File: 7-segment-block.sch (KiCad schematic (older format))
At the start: 5 parts, among them J1 DATA_OUT, J2 DATA_IN, U1 TPIC6C596PWR

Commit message: Add mounting holes, dropper resistors and a buffer
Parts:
- added MK1, MK2, MK3, MK4: Mounting_Hole, Mounting_Holes:MountingHole_3.2mm_M3, symbol Mechanical:Mounting_Hole
- added R1, R2, R3, R4, R5, R6, R7, R8: 100, Resistors_SMD:R_0805_HandSoldering, symbol device:R_Small
- added U?: 74LS125, Housings_SOIC:SOIC-14_3.9x8.7mm_Pitch1.27mm, symbol Logic_74xx:74LS125
- added U? (x3): 74LS125, symbol Logic_74xx:74LS125
- C1: footprint (none) -> Capacitors_SMD:C_0805_HandSoldering; Distributor (none) -> ?; Manufacturer (none) -> ?; PartNo (none) -> ?
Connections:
- net GND: now also J1.7 (Pin_7), J2.7 (Pin_7), U?.1, U?.10, U?.13, U?.4; no longer J1.8 (Pin_8), J2.8 (Pin_8)
- net RCK: now also U?.5; no longer J1.4 (Pin_4)
- net SRCK: now also U?.9; no longer J1.6 (Pin_6)
- net VCC: now also AFF1.1 (C.A.), AFF1.8 (C.A.)
- net ~G: now also J2.8 (Pin_8), U?.12; no longer J1.7 (Pin_7), J2.7 (Pin_7)
- net at AFF1.10 (g): now also R5.1; no longer U1.11 (DRAIN4)
- net at AFF1.2 (e): now also R4.1; no longer U1.6 (DRAIN3)
- net at AFF1.3 (d): now also R3.1; no longer U1.5 (DRAIN2)
- net at AFF1.4 (c): now also R2.1; no longer U1.4 (DRAIN1)
- net at AFF1.5 (DP): now also R1.1; no longer U1.3 (DRAIN0)
- net at AFF1.6 (b): now also R8.1; no longer U1.14 (DRAIN7)
- net at AFF1.7 (a): now also R7.1; no longer U1.13 (DRAIN6)
- net at AFF1.9 (f): now also R6.1; no longer U1.12 (DRAIN5)
- net at U1.9 (SER_OUT): now also U?.2; no longer J1.2 (Pin_2)
- new net: R5.2, U1.11 (DRAIN4)
- new net: R6.2, U1.12 (DRAIN5)
- new net: R7.2, U1.13 (DRAIN6)
- new net: R8.2, U1.14 (DRAIN7)
- new net: R1.2, U1.3 (DRAIN0)
- new net: R2.2, U1.4 (DRAIN1)
- new net: R3.2, U1.5 (DRAIN2)
- new net: R4.2, U1.6 (DRAIN3)
- new net: J1.2 (Pin_2), U?.3
- new net: J1.4 (Pin_4), U?.6
- new net: J1.6 (Pin_6), U?.8
- new net: J1.8 (Pin_8), U?.11
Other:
- moved on the sheet: AFF1, C1, J1, J2, U1

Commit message: Add terminator resistors
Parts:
- added R? (x4): 100, Resistors_SMD:R_0805_HandSoldering, symbol device:R_Small
- gave numbers to parts that had none: 1
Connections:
- net at J1.2 (Pin_2): now also R?.2; no longer U2.3
- net at J1.4 (Pin_4): now also R?.2; no longer U2.6
- net at J1.6 (Pin_6): now also R?.2; no longer U2.8
- net at J1.8 (Pin_8): now also R?.2; no longer U2.11
- new net: R?.1, U2.3
- new net: R?.1, U2.6
- new net: R?.1, U2.8
- new net: R?.1, U2.11
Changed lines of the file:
@@
 $EndComp
 $Comp
-L Logic_74xx:74LS125 U?
+L Logic_74xx:74LS125 U2
 U 1 1 5A146F5B
 P 2000 3500
-F 0 "U?" H 2000 3817 50  0000 C CNN
+F 0 "U2" H 2000 3817 50  0000 C CNN
 F 1 "74LS125" H 2000 3726 50  0000 C CNN
 F 2 "Housings_SOIC:SOIC-14_3.9x8.7mm_Pitch1.27mm" H 2000 3500 50  0001 C CNN
@@
 $EndComp
 $Comp
-L Logic_74xx:74LS125 U?
+L Logic_74xx:74LS125 U2
 U 2 1 5A14756A
 P 2000 4150
-F 0 "U?" H 2000 4467 50  0000 C CNN
+F 0 "U2" H 2000 4467 50  0000 C CNN
 F 1 "74LS125" H 2000 4376 50  0000 C CNN
 F 2 "" H 2000 4150 50  0001 C CNN
@@
 $EndComp
 $Comp
-L Logic_74xx:74LS125 U?
+L Logic_74xx:74LS125 U2
 U 3 1 5A14764F
 P 2000 4800
-F 0 "U?" H 2000 5117 50  0000 C CNN
+F 0 "U2" H 2000 5117 50  0000 C CNN
 F 1 "74LS125" H 2000 5026 50  0000 C CNN
 F 2 "" H 2000 4800 50  0001 C CNN
@@
 $EndComp
 $Comp
-L Logic_74xx:74LS125 U?
+L Logic_74xx:74LS125 U2
 U 4 1 5A147742
 P 2000 5500
-F 0 "U?" H 2000 5817 50  0000 C CNN
+F 0 "U2" H 2000 5817 50  0000 C CNN
 F 1 "74LS125" H 2000 5726 50  0000 C CNN
 F 2 "" H 2000 5500 50  0001 C CNN
@@
 $EndComp
 $Comp
-L power:GND #PWR?
+L power:GND #PWR08
 U 1 1 5A14EE66
 P 2650 5750
-F 0 "#PWR?" H 2650 5500 50  0001 C CNN
+F 0 "#PWR08" H 2650 5500 50  0001 C CNN
 F 1 "GND" H 2655 5577 50  0000 C CNN
 F 2 "" H 2650 5750 50  0001 C CNN
@@
 Connection ~ 2650 4400
 Wire Wire Line
-	1700 3500 900  3500
-Wire Wire Line
 	1700 4150 1700 3700
 Wire Wire Line
-	1700 3700 900  3700
-Wire Wire Line
 	1700 4800 1550 4800
 Wire Wire Line
 	1550 4800 1550 3900
-Wire Wire Line
-	1550 3900 900  3900
 Wire Wire Line
 	3900 4000 4450 4000
@@
 Wire Wire Line
 	1400 5500 1400 4100
-Wire Wire Line
-	1400 4100 900  4100
-$Comp
-L power:+5V #PWR?
+$Comp
+L power:+5V #PWR09
 U 1 1 5A16B1E5
 P 1450 3250
-F 0 "#PWR?" H 1450 3100 50  0001 C CNN
+F 0 "#PWR09" H 1450 3100 50  0001 C CNN
 F 1 "+5V" H 1465 3423 50  0000 C CNN
 F 2 "" H 1450 3250 50  0001 C CNN
@@
 	1450 3400 1450 3250
 $Comp
-L power:VCC #PWR?
+L power:VCC #PWR010
 U 1 1 5A16B22C
 P 1250 3250
-F 0 "#PWR?" H 1250 3100 50  0001 C CNN
+F 0 "#PWR010" H 1250 3100 50  0001 C CNN
 F 1 "VCC" H 1267 3423 50  0000 C CNN
 F 2 "" H 1250 3250 50  0001 C CNN
@@
 Connection ~ 1250 4200
 $Comp
-L power:GND #PWR?
+L power:GND #PWR011
 U 1 1 5A171A26
 P 1050 4500
-F 0 "#PWR?" H 1050 4250 50  0001 C CNN
+F 0 "#PWR011" H 1050 4250 50  0001 C CNN
 F 1 "GND" H 1055 4327 50  0000 C CNN
 F 2 "" H 1050 4500 50  0001 C CNN
@@
 	900  4000 1050 4000
 Connection ~ 1050 4000
+$Comp
+L device:R_Small R?
+U 1 1 5A17D638
+P 1000 3500
+F 0 "R?" V 950 3500 50  0000 C CNN
+F 1 "100" V 950 3650 50  0000 C CNN
+F 2 "Resistors_SMD:R_0805_HandSoldering" H 1000 3500 50  0001 C CNN
+F 3 "" H 1000 3500 50  0001 C CNN
+F 4 "?" H 1000 3500 60  0001 C CNN "PartNo"
+F 5 "?" H 1000 3500 60  0001 C CNN "Manufacturer"
+F 6 "?" H 1000 3500 60  0001 C CNN "Distributor"
+	1    1000 3500
+	0    1    1    0
+$EndComp
+$Comp
+L device:R_Small R?
+U 1 1 5A17D6EE
+P 1000 3700
+F 0 "R?" V 950 3700 50  0000 C CNN
+F 1 "100" V 950 3850 50  0000 C CNN
+F 2 "Resistors_SMD:R_0805_HandSoldering" H 1000 3700 50  0001 C CNN
+F 3 "" H 1000 3700 50  0001 C CNN
+F 4 "?" H 1000 3700 60  0001 C CNN "PartNo"
+F 5 "?" H 1000 3700 60  0001 C CNN "Manufacturer"
+F 6 "?" H 1000 3700 60  0001 C CNN "Distributor"
+	1    1000 3700
+	0    1    1    0
+$EndComp
+$Comp
+L device:R_Small R?
+U 1 1 5A17D736
+P 1000 3900
+F 0 "R?" V 950 3900 50  0000 C CNN
+F 1 "100" V 950 4050 50  0000 C CNN
+F 2 "Resistors_SMD:R_0805_HandSoldering" H 1000 3900 50  0001 C CNN
+F 3 "" H 1000 3900 50  0001 C CNN
+F 4 "?" H 1000 3900 60  0001 C CNN "PartNo"
+F 5 "?" H 1000 3900 60  0001 C CNN "Manufacturer"
+F 6 "?" H 1000 3900 60  0001 C CNN "Distributor"
+	1    1000 3900
+	0    1    1    0
+$EndComp
+$Comp
+L device:R_Small R?
+U 1 1 5A17D784
+P 1000 4100
+F 0 "R?" V 950 4100 50  0000 C CNN
+F 1 "100" V 950 4250 50  0000 C CNN
+F 2 "Resistors_SMD:R_0805_HandSoldering" H 1000 4100 50  0001 C CNN
+F 3 "" H 1000 4100 50  0001 C CNN
+F 4 "?" H 1000 4100 60  0001 C CNN "PartNo"
+F 5 "?" H 1000 4100 60  0001 C CNN "Manufacturer"
+F 6 "?" H 1000 4100 60  0001 C CNN "Distributor"
+	1    1000 4100
+	0    1    1    0
+$EndComp
+Wire Wire Line
+	1100 3500 1700 3500
+Wire Wire Line
+	1100 3700 1700 3700
+Wire Wire Line
+	1100 3900 1550 3900
+Wire Wire Line
+	1100 4100 1400 4100
 $EndSCHEMATC

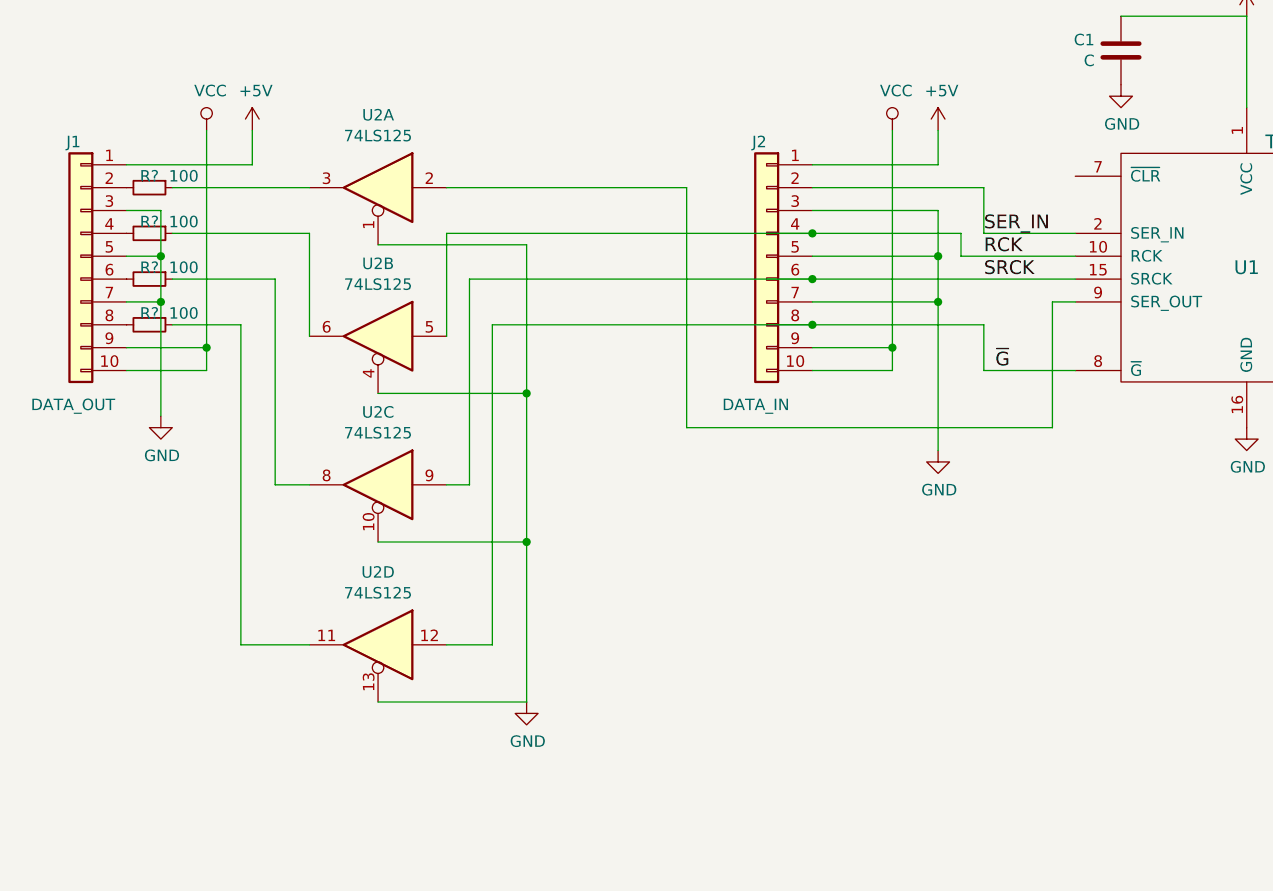
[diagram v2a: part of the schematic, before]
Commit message: Start routing, maybe change to a different buffer that has a more friendly pin location
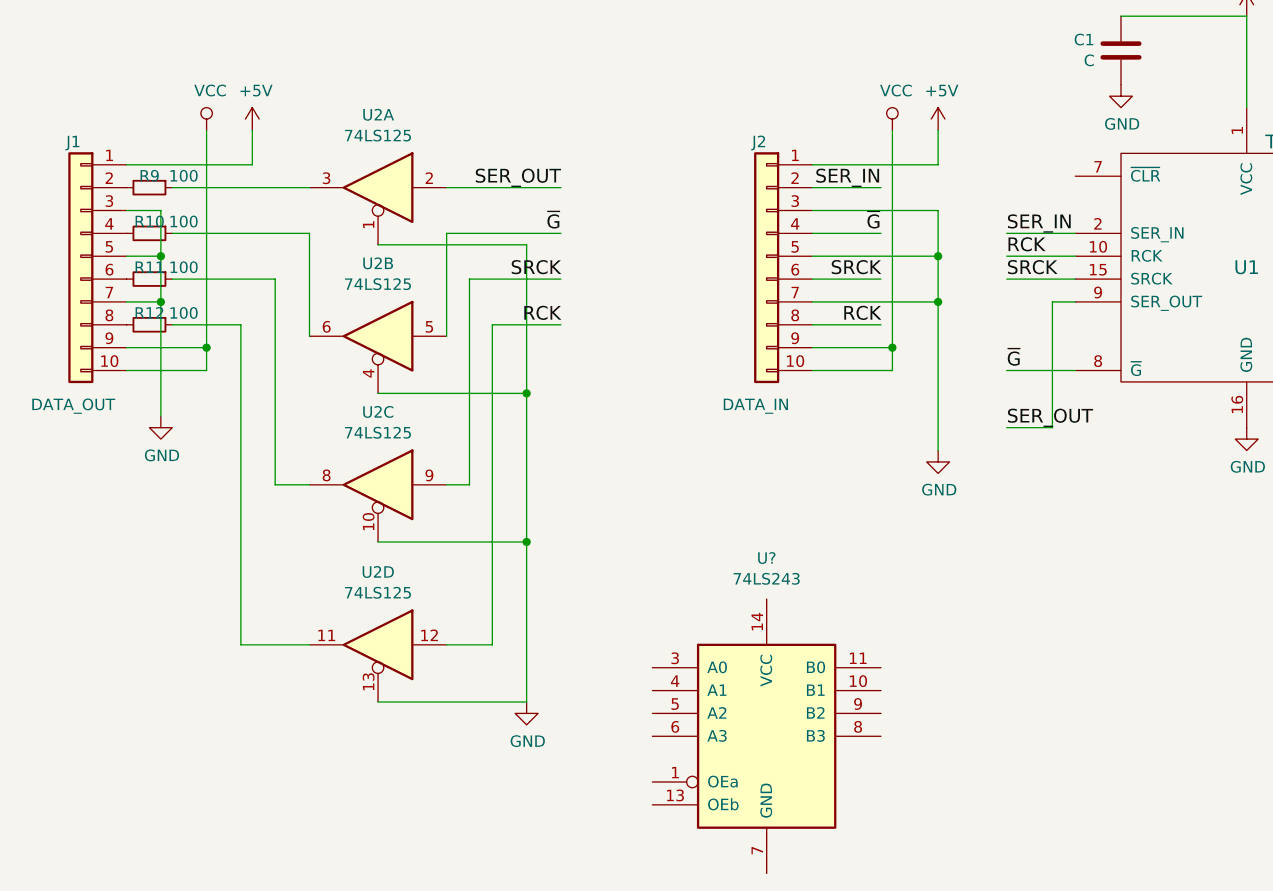
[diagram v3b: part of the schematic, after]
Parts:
- added U?: 74LS243, symbol Logic_74xx:74LS243
- gave numbers to parts that had none: 4
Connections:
- net RCK: now also J2.8 (Pin_8), U2.12; no longer J2.4 (Pin_4), U2.5
- net ~G: now also J2.4 (Pin_4), U2.5; no longer J2.8 (Pin_8), U2.12
- net SER_OUT: now reaches U1.9 (SER_OUT), U2.2
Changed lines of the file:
@@
 	-1   0    0    -1
 $EndComp
-Text Label 4650 3700 0    60   ~ 0
+Text Label 4750 3700 0    60   ~ 0
 SER_IN
-Text Label 4650 3800 0    60   ~ 0
+Text Label 4750 3800 0    60   ~ 0
 RCK
-Text Label 4650 3900 0    60   ~ 0
+Text Label 4750 3900 0    60   ~ 0
 SRCK
-Text Label 4700 4300 0    60   ~ 0
+Text Label 4750 4300 0    60   ~ 0
 ~G
 $Comp
@@
 	5800 2750 5800 3150
 Wire Wire Line
-	2400 3900 5050 3900
-Wire Wire Line
 	3900 3800 4450 3800
 Wire Wire Line
@@
 Connection ~ 4450 3800
 Wire Wire Line
-	2300 3700 4550 3700
-Wire Wire Line
-	4550 3700 4550 3800
-Wire Wire Line
-	4550 3800 5050 3800
-Wire Wire Line
-	3900 3500 4650 3500
-Wire Wire Line
-	4650 3500 4650 3700
-Wire Wire Line
-	4650 3700 5050 3700
-Wire Wire Line
-	5050 4300 4650 4300
-Wire Wire Line
-	4650 4300 4650 4100
+	3900 3700 4200 3700
+Wire Wire Line
+	4750 3800 5050 3800
+Wire Wire Line
+	3900 3500 4200 3500
+Wire Wire Line
+	4750 3700 5050 3700
+Wire Wire Line
+	5050 4300 4750 4300
 Wire Wire Line
 	4450 3600 4450 4650
@@
 	4950 4000 4950 4550
 Wire Wire Line
-	4950 4550 3350 4550
-Wire Wire Line
-	3350 4550 3350 3500
-Wire Wire Line
-	2300 3500 3350 3500
-Connection ~ 3900 3700
-Connection ~ 3900 3900
+	4750 4550 4950 4550
+Wire Wire Line
+	2300 3500 2800 3500
 Wire Wire Line
 	9100 3250 9100 3650
@@
 Connection ~ 4450 4000
 Wire Wire Line
-	2500 4100 4650 4100
-Connection ~ 3900 4100
+	3900 4100 4200 4100
 Wire Wire Line
 	1700 5500 1400 5500
@@
 Connection ~ 1050 4000
 $Comp
-L device:R_Small R?
+L device:R_Small R9
 U 1 1 5A17D638
 P 1000 3500
-F 0 "R?" V 950 3500 50  0000 C CNN
+F 0 "R9" V 950 3500 50  0000 C CNN
 F 1 "100" V 950 3650 50  0000 C CNN
 F 2 "Resistors_SMD:R_0805_HandSoldering" H 1000 3500 50  0001 C CNN
@@
 $EndComp
 $Comp
-L device:R_Small R?
+L device:R_Small R10
 U 1 1 5A17D6EE
 P 1000 3700
-F 0 "R?" V 950 3700 50  0000 C CNN
+F 0 "R10" V 950 3700 50  0000 C CNN
 F 1 "100" V 950 3850 50  0000 C CNN
 F 2 "Resistors_SMD:R_0805_HandSoldering" H 1000 3700 50  0001 C CNN
@@
 $EndComp
 $Comp
-L device:R_Small R?
+L device:R_Small R11
 U 1 1 5A17D736
 P 1000 3900
-F 0 "R?" V 950 3900 50  0000 C CNN
+F 0 "R11" V 950 3900 50  0000 C CNN
 F 1 "100" V 950 4050 50  0000 C CNN
 F 2 "Resistors_SMD:R_0805_HandSoldering" H 1000 3900 50  0001 C CNN
@@
 $EndComp
 $Comp
-L device:R_Small R?
+L device:R_Small R12
 U 1 1 5A17D784
 P 1000 4100
-F 0 "R?" V 950 4100 50  0000 C CNN
+F 0 "R12" V 950 4100 50  0000 C CNN
 F 1 "100" V 950 4250 50  0000 C CNN
 F 2 "Resistors_SMD:R_0805_HandSoldering" H 1000 4100 50  0001 C CNN
@@
 Wire Wire Line
 	1100 4100 1400 4100
+Text Label 4750 4550 0    60   ~ 0
+SER_OUT
+Text Label 2800 3500 2    60   ~ 0
+SER_OUT
+Wire Wire Line
+	4750 3900 5050 3900
+Text Label 4200 3900 2    60   ~ 0
+SRCK
+Text Label 4200 4100 2    60   ~ 0
+RCK
+Text Label 4200 3500 2    60   ~ 0
+SER_IN
+Text Label 2800 4100 2    60   ~ 0
+RCK
+Wire Wire Line
+	2800 3700 2300 3700
+Wire Wire Line
+	2400 3900 2800 3900
+Wire Wire Line
+	4200 3900 3900 3900
+Text Label 2800 3900 2    60   ~ 0
+SRCK
+Text Label 4200 3700 2    60   ~ 0
+~G
+Wire Wire Line
+	2500 4100 2800 4100
+Text Label 2800 3700 2    60   ~ 0
+~G
+$Comp
+L Logic_74xx:74LS243 U?
+U 1 1 5A1AFDE1
+P 3700 5900
+F 0 "U?" H 3700 6678 50  0000 C CNN
+F 1 "74LS243" H 3700 6587 50  0000 C CNN
+F 2 "" H 3700 5900 50  0001 C CNN
+F 3 "http://www.ti.com/lit/gpn/sn74LS243" H 3700 5900 50  0001 C CNN
+	1    3700 5900
+	1    0    0    -1
+$EndComp
 $EndSCHEMATC
